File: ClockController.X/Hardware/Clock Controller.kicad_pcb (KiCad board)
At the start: 2 copper layers, 63.5 x 44.5 mm, 47 parts, among them J1 UJC-VP-3-SMT-TR, J2 HDR-1X2H, Q1 DMG7430LFG-7, Q2 FDD7N25LZTM, Q3 MMBT2222A-TP, Q4 MMBT2907ALT1G, Q5 MMBT2222A-TP, Q6 MMBT2222A-TP, U1 PIC16F15224-I/SL, U2 AS78L05RTR-E1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

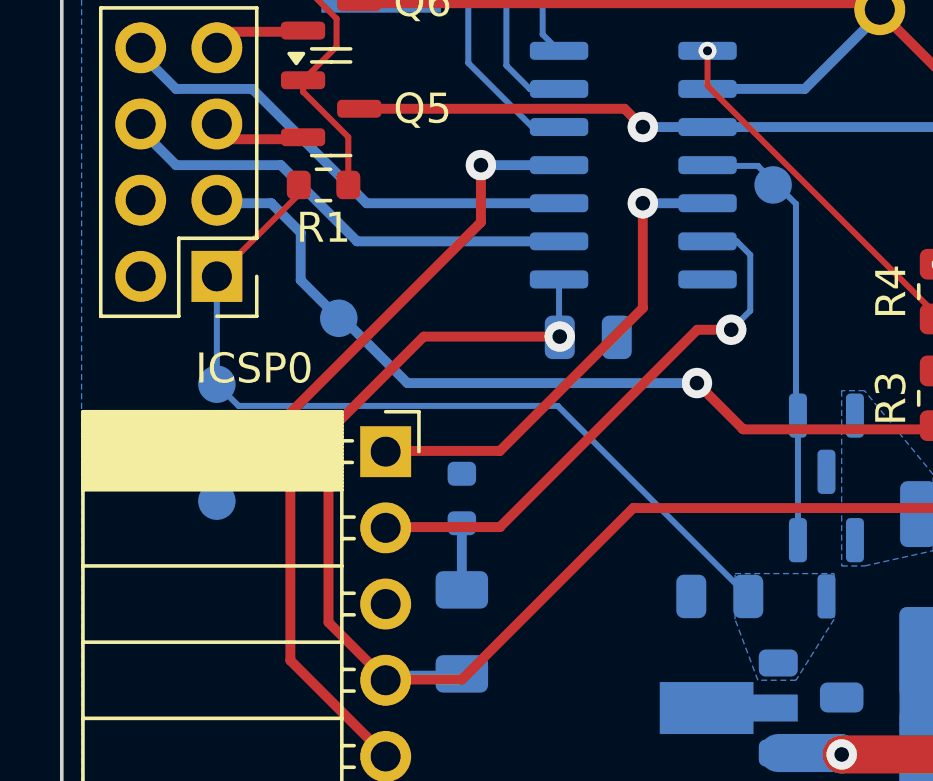
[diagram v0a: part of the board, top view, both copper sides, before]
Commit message: Relocated the test points
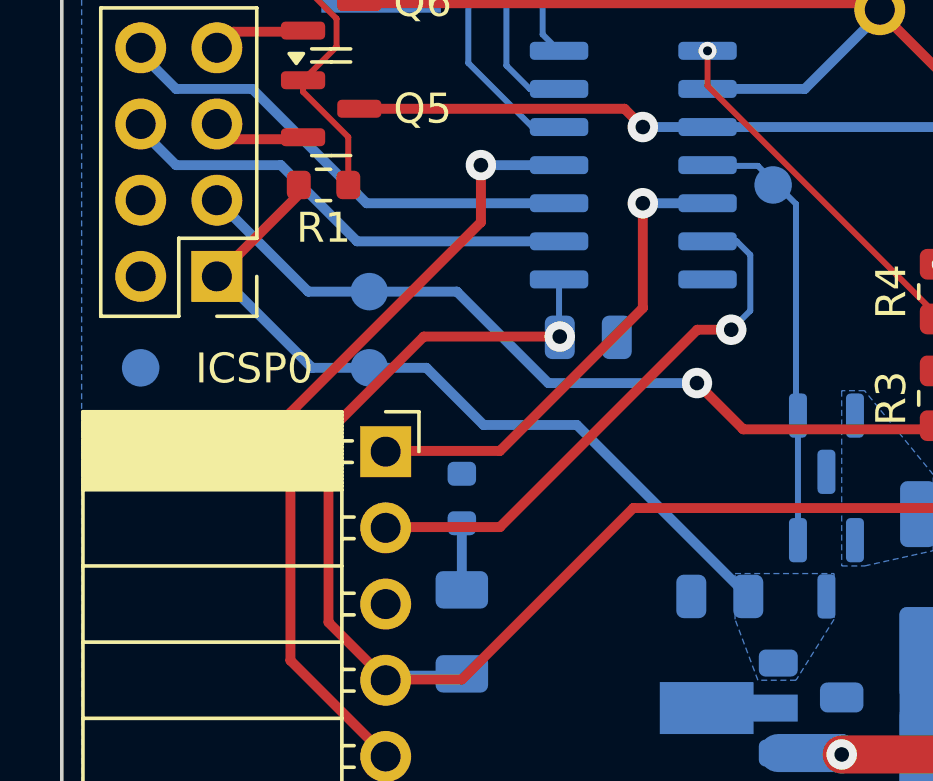
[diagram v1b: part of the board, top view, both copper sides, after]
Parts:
- moved GND0 5.12 mm to (119.4, 111.8)
- moved Vcc0 5.11 mm to (127.0, 111.8)
- moved Vnn0 1.35 mm to (127.0, 109.2)
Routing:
- net +5V: track 28.4 -> 26.3 mm
- net VNN: track 31.3 -> 30.3 mm
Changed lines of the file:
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@@
 	(footprint "Clock Controller:TP_1.25MM"
 		(layer "B.Cu")
-		(at 121.92 116.205 180)
+		(at 119.38 111.76 180)
 		(property "Reference" "GND0"
 			(at 0 0 0)
@@
 	(footprint "Clock Controller:TP_1.25MM"
 		(layer "B.Cu")
-		(at 125.984 110.109 90.001)
+		(at 127 109.22 90.001)
 		(property "Reference" "Vnn0"
 			(at 0 0 90.001)
@@
 	(footprint "Clock Controller:TP_1.25MM"
 		(layer "B.Cu")
-		(at 121.92 112.3061 180)
+		(at 127 111.76 180)
 		(property "Reference" "Vcc0"
 			(at 0 0 0)
@@
 		)
 	)
-	(gr_text "Vcc"
-		(at 123.825 114.681 0)
+	(gr_text "Vnn"
+		(at 131.445 109.855 0)
 		(layer "B.SilkS")
 		(effects
@@
 		)
 	)
-	(gr_text "Vnn"
-		(at 127.762 108.966 0)
+	(gr_text "Vcc"
+		(at 131.445 112.395 0)
 		(layer "B.SilkS")
 		(effects
@@
 	)
 	(gr_text "GND"
-		(at 124.206 118.745 360)
+		(at 124.46 112.395 360)
 		(layer "B.SilkS")
 		(effects
@@
 		(start 121.92 108.712)
 		(end 124.651 105.981)
-		(width 0.2)
+		(width 0.33)
 		(layer "F.Cu")
 		(net 2)
@@
 		(start 124.651 105.981)
 		(end 124.651 105.664014)
-		(width 0.2)
+		(width 0.33)
 		(layer "F.Cu")
 		(net 2)
 	)
 	(segment
-		(start 122.6439 113.03)
-		(end 121.92 112.3061)
-		(width 0.2)
+		(start 125.095 111.76)
+		(end 122.047 108.712)
+		(width 0.33)
 		(layer "B.Cu")
 		(net 2)
 	)
 	(segment
-		(start 121.92 112.3061)
-		(end 121.92 108.712)
-		(width 0.2)
+		(start 127 111.76)
+		(end 125.095 111.76)
+		(width 0.33)
 		(layer "B.Cu")
 		(net 2)
 	)
 	(segment
-		(start 133.284035 113.03)
-		(end 122.6439 113.03)
-		(width 0.2)
+		(start 128.905 111.76)
+		(end 127 111.76)
+		(width 0.33)
+		(layer "B.Cu")
+		(net 2)
+	)
+	(segment
+		(start 133.919035 113.665)
+		(end 130.81 113.665)
+		(width 0.33)
+		(layer "B.Cu")
+		(net 2)
+	)
+	(segment
+		(start 130.81 113.665)
+		(end 128.905 111.76)
+		(width 0.33)
 		(layer "B.Cu")
 		(net 2)
@@
 	(segment
 		(start 139.634 119.379965)
-		(end 133.284035 113.03)
-		(width 0.2)
+		(end 133.919035 113.665)
+		(width 0.33)
+		(layer "B.Cu")
+		(net 2)
+	)
+	(segment
+		(start 122.047 108.712)
+		(end 121.92 108.712)
+		(width 0.33)
 		(layer "B.Cu")
 		(net 2)
@@
 	)
 	(segment
-		(start 137.922 112.268)
-		(end 128.27 112.268)
+		(start 129.921 109.22)
+		(end 127 109.22)
 		(width 0.33)
 		(layer "B.Cu")
@@
 	)
 	(segment
-		(start 128.27 112.268)
-		(end 126.0856 110.0836)
-		(width 0.33)
-		(layer "B.Cu")
-		(net 19)
-	)
-	(segment
-		(start 126.0856 110.0836)
-		(end 126.0094 110.0836)
-		(width 0.33)
-		(layer "B.Cu")
-		(net 19)
-	)
-	(segment
-		(start 124.714 108.839)
-		(end 125.984 110.109)
-		(width 0.33)
-		(layer "B.Cu")
-		(net 19)
-	)
-	(segment
-		(start 121.8311 106.2736)
-		(end 123.7361 106.2736)
+		(start 137.922 112.268)
+		(end 132.969 112.268)
 		(width 0.33)
 		(layer "B.Cu")
@@
 	)
 	(segment
-		(start 124.714 107.2515)
-		(end 124.714 108.839)
+		(start 127 109.22)
+		(end 124.968 109.22)
 		(width 0.33)
 		(layer "B.Cu")
@@
 	)
 	(segment
-		(start 126.0094 110.0836)
-		(end 125.984 110.109)
+		(start 124.968 109.22)
+		(end 121.92 106.172)
 		(width 0.33)
 		(layer "B.Cu")
@@
 	)
 	(segment
-		(start 123.7361 106.2736)
-		(end 124.714 107.2515)
+		(start 132.969 112.268)
+		(end 129.921 109.22)
 		(width 0.33)
 		(layer "B.Cu")

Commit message: Add JLPCB order placeholder
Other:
- board text added: "JLCJLCJLCJLC"
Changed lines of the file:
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@@
 		(layer "B.Fab")
+	)
+	(gr_text "JLCJLCJLCJLC"
+		(at 178.435 104.775 270)
+		(layer "F.SilkS")
+		(effects
+			(font
+				(size 1 1)
+				(thickness 0.3)
+				(bold yes)
+			)
+			(justify bottom)
+		)
 	)
 	(gr_text "Nixie Clock Controller (v1.1)\nAaron Johnson\n4/4/2026"
@@
 	)
 	(segment
+		(start 127.5461 122.1486)
+		(end 150.9014 122.1486)
+		(width 0.33)
+		(layer "F.Cu")
+		(net 17)
+	)
+	(segment
+		(start 144.463267 94.742)
+		(end 161.392367 111.6711)
+		(width 0.33)
+		(layer "F.Cu")
+		(net 17)
+	)
+	(segment
+		(start 144.018047 94.80558)
+		(end 144.018047 94.742)
+		(width 0.33)
+		(layer "F.Cu")
+		(net 17)
+	)
+	(segment
+		(start 125.6411 120.2436)
+		(end 127.5461 122.1486)
+		(width 0.33)
+		(layer "F.Cu")
+		(net 17)
+	)
+	(segment
 		(start 133.35 110.7186)
 		(end 128.8161 110.7186)
@@
 	)
 	(segment
-		(start 135.8011 116.4336)
-		(end 150.7236 116.4336)
-		(width 0.33)
-		(layer "F.Cu")
-		(net 17)
-	)
-	(segment
-		(start 130.0861 122.1486)
-		(end 135.8011 116.4336)
-		(width 0.33)
-		(layer "F.Cu")
-		(net 17)
-	)
-	(segment
-		(start 144.018047 94.742)
-		(end 144.654533 94.742)
-		(width 0.33)
-		(layer "F.Cu")
-		(net 17)
-	)
-	(segment
-		(start 144.018047 94.80558)
-		(end 144.018047 94.742)
-		(width 0.33)
-		(layer "F.Cu")
-		(net 17)
-	)
-	(segment
-		(start 127.5461 122.1486)
-		(end 130.0861 122.1486)
-		(width 0.33)
-		(layer "F.Cu")
-		(net 17)
-	)
-	(segment
-		(start 144.654533 94.742)
-		(end 161.583633 111.6711)
-		(width 0.33)
-		(layer "F.Cu")
-		(net 17)
-	)
-	(segment
-		(start 161.583633 111.6711)
+		(start 161.392367 111.6711)
 		(end 167.2336 111.6711)
+		(width 0.33)
+		(layer "F.Cu")
+		(net 17)
+	)
+	(segment
+		(start 125.6411 113.8936)
+		(end 125.6411 120.2436)
 		(width 0.33)
 		(layer "F.Cu")
@@
 	)
 	(segment
-		(start 125.6411 120.2436)
-		(end 127.5461 122.1486)
+		(start 150.9014 122.1486)
+		(end 161.3789 111.6711)
+		(width 0.33)
+		(layer "F.Cu")
+		(net 17)
+	)
+	(segment
+		(start 144.018047 94.742)
+		(end 144.463267 94.742)
 		(width 0.33)
 		(layer "F.Cu")
@@
 	)
 	(segment
-		(start 125.6411 113.8936)
-		(end 125.6411 120.2436)
-		(width 0.33)
-		(layer "F.Cu")
-		(net 17)
-	)
-	(segment
-		(start 155.4861 111.6711)
+		(start 161.3789 111.6711)
 		(end 167.2336 111.6711)
-		(width 0.33)
-		(layer "F.Cu")
-		(net 17)
-	)
-	(segment
-		(start 150.7236 116.4336)
-		(end 155.4861 111.6711)
 		(width 0.33)
 		(layer "F.Cu")
@@
 	)
 	(segment
-		(start 129.921 109.22)
+		(start 128.905 109.22)
 		(end 127 109.22)
 		(width 0.33)
@@
 	(segment
 		(start 137.922 112.268)
-		(end 132.969 112.268)
+		(end 131.953 112.268)
 		(width 0.33)
 		(layer "B.Cu")
@@
 	)
 	(segment
-		(start 132.969 112.268)
-		(end 129.921 109.22)
-		(width 0.33)
-		(layer "B.Cu")
+		(start 131.953 112.268)
+		(end 128.905 109.22)
+		(width 0.33)
+		(layer "B.Cu")

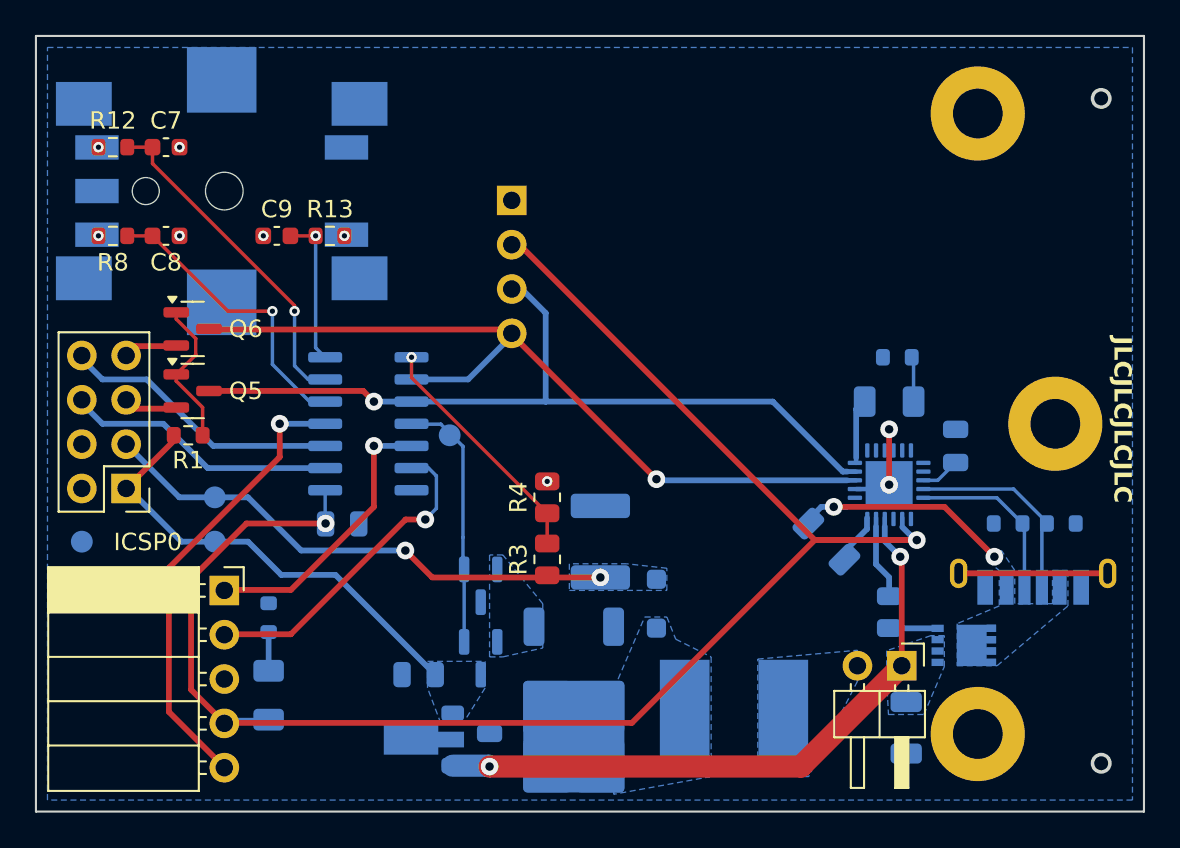
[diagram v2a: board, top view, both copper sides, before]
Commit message: 4-layer board
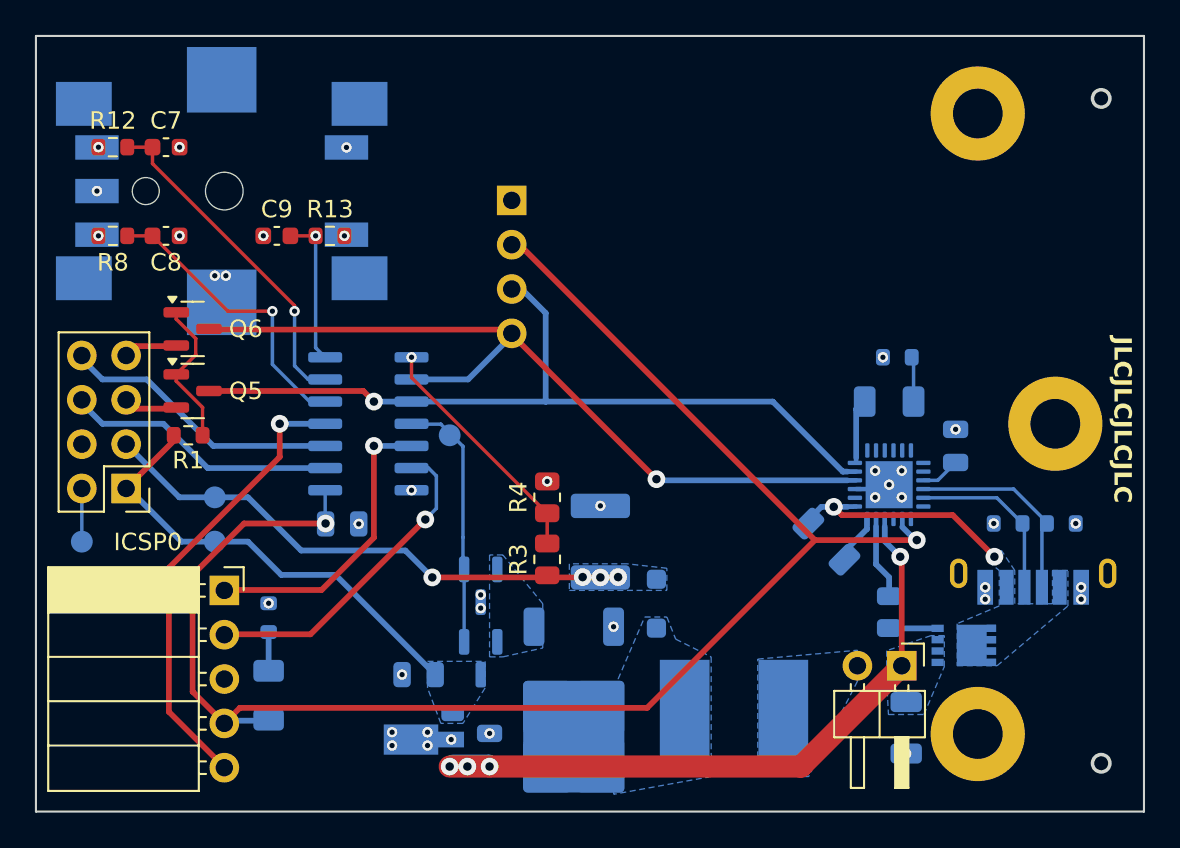
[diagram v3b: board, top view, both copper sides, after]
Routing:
- net GND: track 13.9 -> 5.19 mm, vias 6 -> 36
- net V5V: track 98.6 -> 92.8 mm
- net +20V: track 37.0 -> 39.3 mm, vias 2 -> 4
- net /Microcontroller/ICSPCLK: track 16.1 -> 17.2 mm
- net VNN: track 30.3 -> 31.4 mm, vias 2 -> 4
- added copper zone on In2.Cu, net GND
- removed copper zone on B.Cu, net GND
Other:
- copper layers 2 -> 4

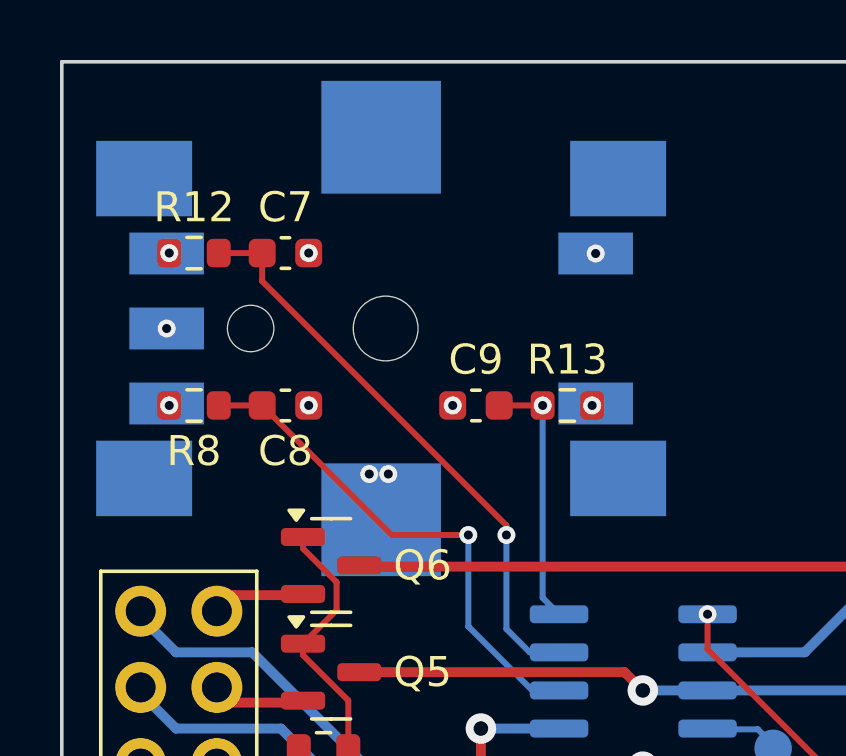
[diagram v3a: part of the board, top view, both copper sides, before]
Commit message: Swapped out a bad footprint that was missing layers
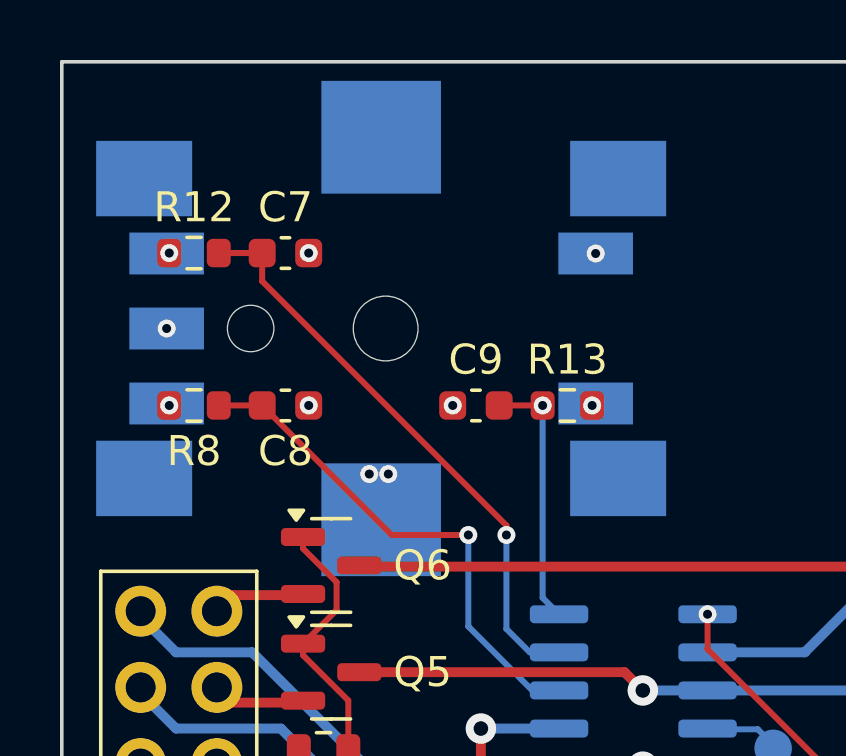
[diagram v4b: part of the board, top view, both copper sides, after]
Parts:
- S1: footprint Clock Controller:IC5_PEC11S-929K-S0015_BRN -> Rotary_Encoder_:PEC11S-929K-S0015

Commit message: Fixed some broken 3d model references
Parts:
- turned Q1 to 0.002 degrees
